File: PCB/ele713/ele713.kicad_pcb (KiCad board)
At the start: 2 copper layers, 37 parts, among them T1 Vi = 36-72V, Vo = 12V / 1.25A, U1 LM5012, U2 LT8304

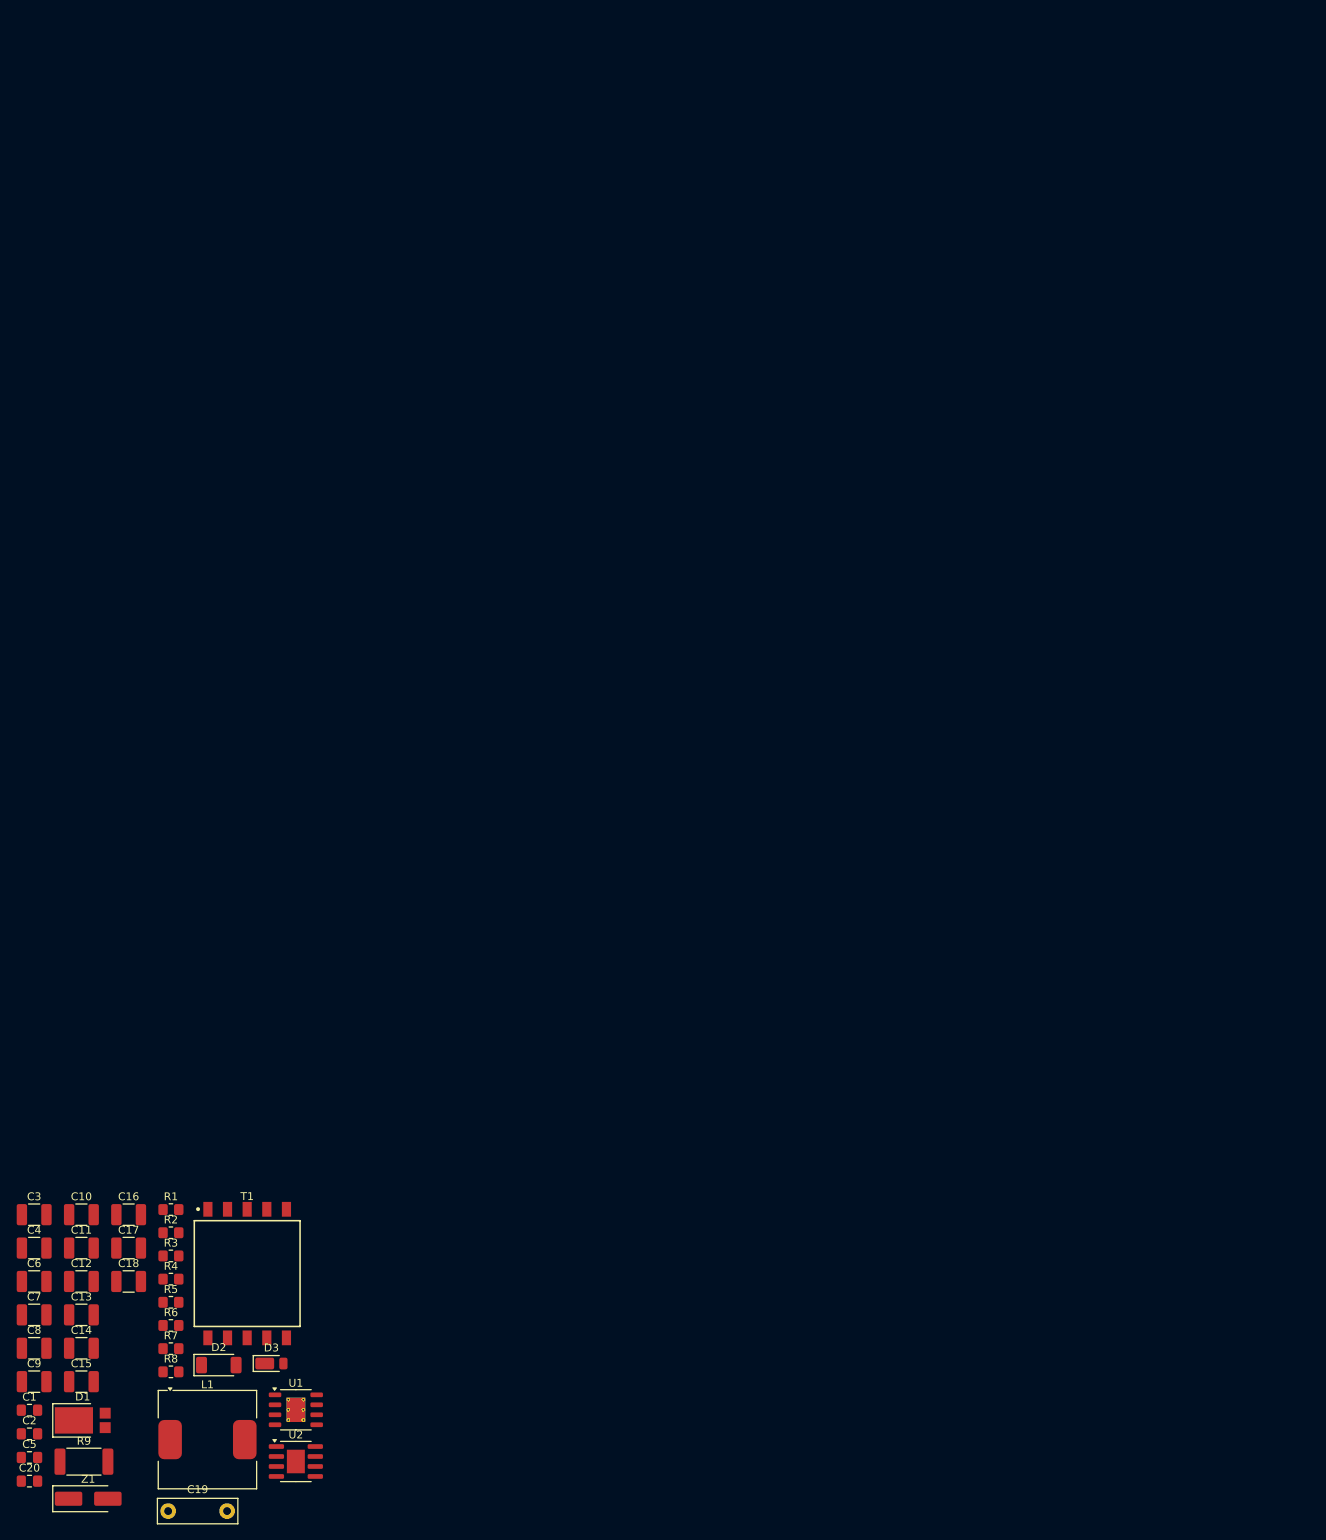
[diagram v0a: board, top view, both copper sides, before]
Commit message: libraries added, schematic fully completed except terminals
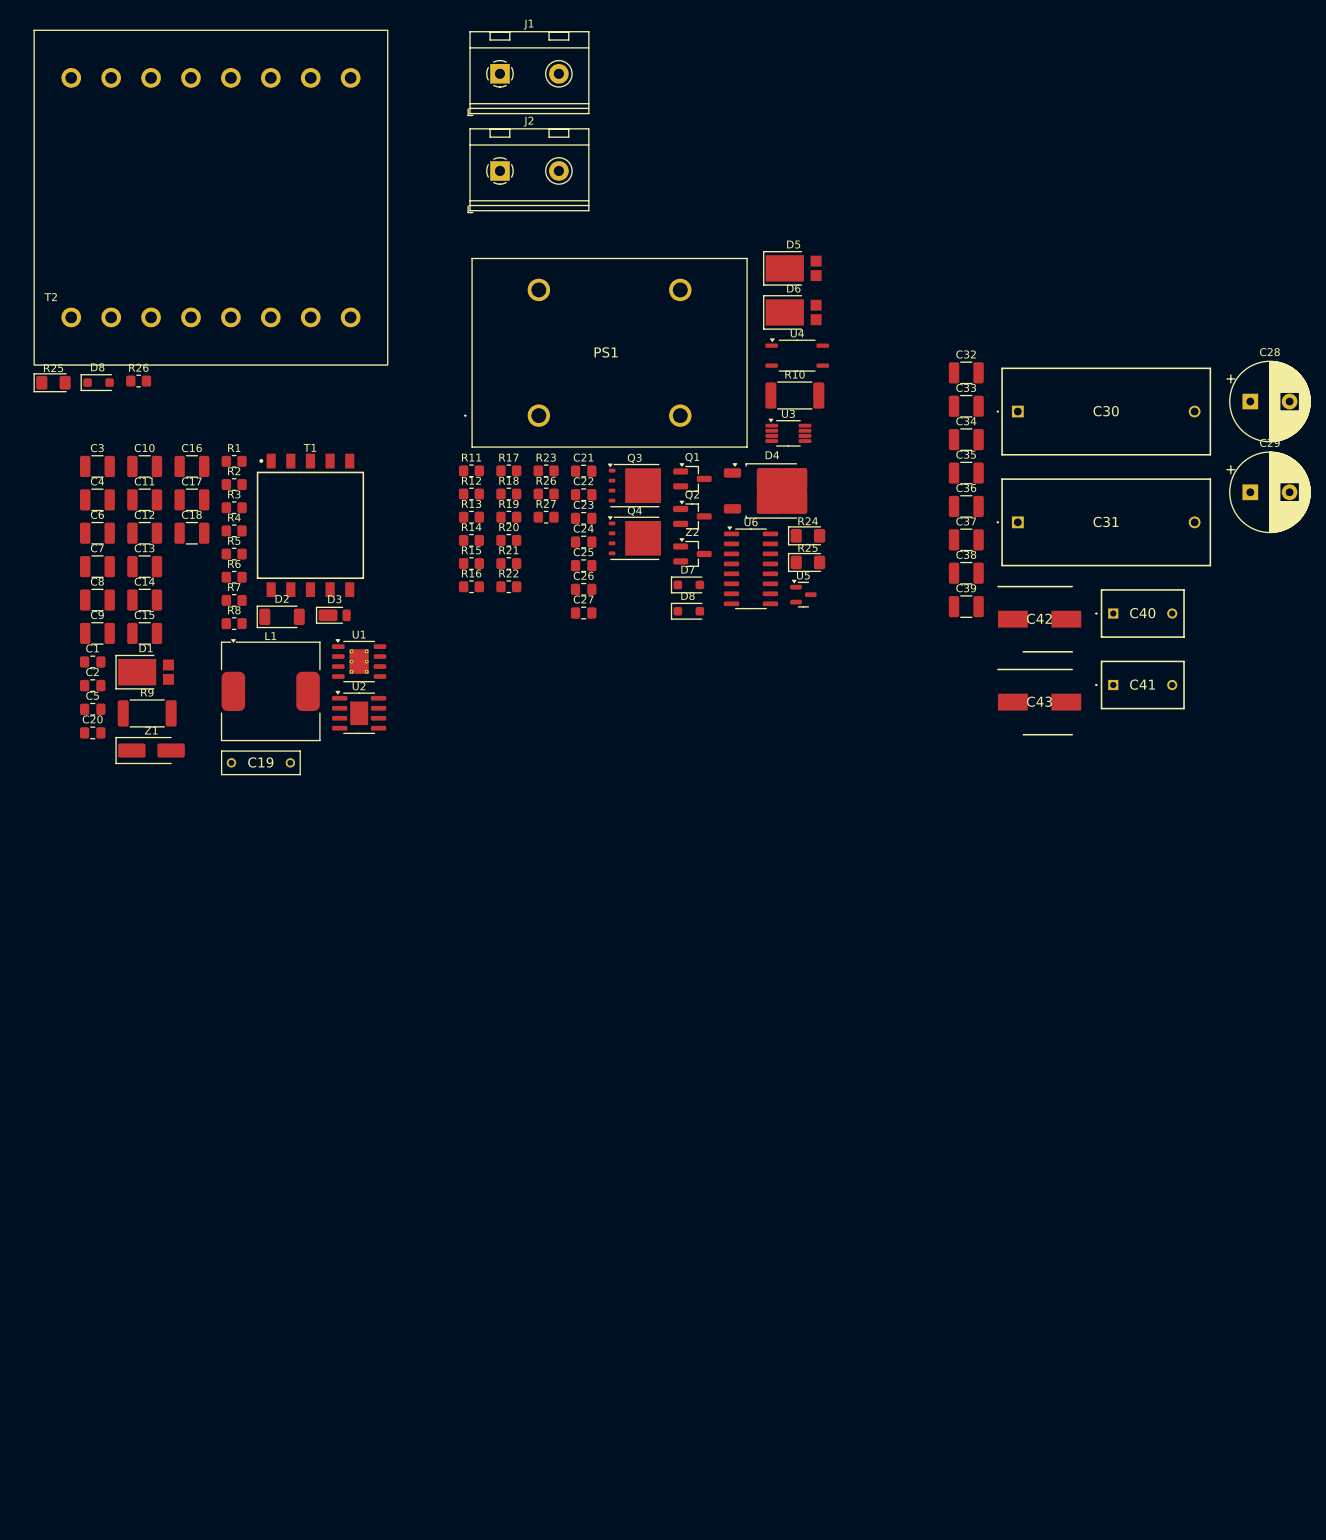
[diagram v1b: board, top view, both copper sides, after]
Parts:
- added C21: 4.7u, Capacitor_SMD:C_0805_2012Metric_Pad1.18x1.45mm_HandSolder, F.Cu at (122.2, -47.9)
- added C22: 6.8n, Capacitor_SMD:C_0805_2012Metric_Pad1.18x1.45mm_HandSolder, F.Cu at (122.2, -44.9)
- added C23: 10n, Capacitor_SMD:C_0805_2012Metric_Pad1.18x1.45mm_HandSolder, F.Cu at (122.2, -41.9)
- added C24: 10n, Capacitor_SMD:C_0805_2012Metric_Pad1.18x1.45mm_HandSolder, F.Cu at (122.2, -38.9)
- added C25: 470p, Capacitor_SMD:C_0805_2012Metric_Pad1.18x1.45mm_HandSolder, F.Cu at (122.2, -35.9)
- added C26: 100p, Capacitor_SMD:C_0805_2012Metric_Pad1.18x1.45mm_HandSolder, F.Cu at (122.2, -32.9)
- added C27: 1u, Capacitor_SMD:C_0805_2012Metric_Pad1.18x1.45mm_HandSolder, F.Cu at (122.2, -29.9)
- added C28: 22u, Capacitor_THT:CP_Radial_D10.0mm_P5.00mm, F.Cu at (207.0, -56.8)
- added C29: 22u, Capacitor_THT:CP_Radial_D10.0mm_P5.00mm, F.Cu at (207.0, -45.2)
- added C30: 3.3u, powerlabLibrary:R46KN410050N1K, F.Cu at (177.4, -55.5)
- added C31: 3.3u, powerlabLibrary:R46KN410050N1K, F.Cu at (177.4, -41.4)
- added C32: 4.7u, Capacitor_SMD:C_1210_3225Metric_Pad1.33x2.70mm_HandSolder, F.Cu at (170.8, -60.4)
- added C33: 4.7u, Capacitor_SMD:C_1210_3225Metric_Pad1.33x2.70mm_HandSolder, F.Cu at (170.8, -56.2)
- added C34: 4.7u, Capacitor_SMD:C_1210_3225Metric_Pad1.33x2.70mm_HandSolder, F.Cu at (170.8, -51.9)
- added C35: 4.7u, Capacitor_SMD:C_1210_3225Metric_Pad1.33x2.70mm_HandSolder, F.Cu at (170.8, -47.7)
- added C36: 22u, Capacitor_SMD:C_1210_3225Metric_Pad1.33x2.70mm_HandSolder, F.Cu at (170.8, -43.4)
- added C37: 22u, Capacitor_SMD:C_1210_3225Metric_Pad1.33x2.70mm_HandSolder, F.Cu at (170.8, -39.2)
- added C38: 22u, Capacitor_SMD:C_1210_3225Metric_Pad1.33x2.70mm_HandSolder, F.Cu at (170.8, -34.9)
- added C39: 22u, Capacitor_SMD:C_1210_3225Metric_Pad1.33x2.70mm_HandSolder, F.Cu at (170.8, -30.7)
- added C40: 2.2u, powerlabLibrary:F861KM473M310A, F.Cu at (189.6, -29.8)
- added C41: 2.2u, powerlabLibrary:F861KM473M310A, F.Cu at (189.6, -20.7)
- added C42: 220u, powerlabLibrary:CAPAE830X1250N, F.Cu at (180.2, -29.1)
- added C43: 220u, powerlabLibrary:CAPAE830X1250N, F.Cu at (180.2, -18.5)
- added D4: V35PWL63, Package_TO_SOT_SMD:TO-252-2, F.Cu at (146.1, -45.4)
- added D5: SDT5H100LP5, powerlabLibrary:D_PowerDI-5, F.Cu at (148.9, -73.7)
- added D6: SDT5H100LP5, powerlabLibrary:D_PowerDI-5, F.Cu at (148.9, -68.1)
- added D7: BZT52H-A18-QX, Diode_SMD:D_SOD-123F, F.Cu at (135.5, -33.5)
- added D8: BZT52H-A18-QX, Diode_SMD:D_SOD-123F, F.Cu at (60.4, -59.2)
- added D8: BZT52H-A18-QX, Diode_SMD:D_SOD-123F, F.Cu at (135.5, -30.1)
- added J1: Conn_01x02_Pin, TerminalBlock_RND:TerminalBlock_RND_205-00067_1x02_P7.50mm_Horizontal, F.Cu at (111.5, -98.5)
- added J2: Conn_01x02_Pin, TerminalBlock_RND:TerminalBlock_RND_205-00067_1x02_P7.50mm_Horizontal, F.Cu at (111.5, -86.1)
- added PS1: SC-18-10J, powerlabLibrary:SC1810J, F.Cu at (116.5, -55.0)
- added Q1: PMBT2222A-Q, Package_TO_SOT_SMD:SOT-23_Handsoldering, F.Cu at (136.0, -47.0)
- added Q2: PMBT2907A-Q, Package_TO_SOT_SMD:SOT-23_Handsoldering, F.Cu at (136.0, -42.2)
- added Q3: BSC096N10LS5, Package_TO_SOT_SMD:TDSON-8-1, F.Cu at (128.7, -46.1)
- added Q4: BSC096N10LS5, Package_TO_SOT_SMD:TDSON-8-1, F.Cu at (128.7, -39.4)
- added R10: 4m, Resistor_SMD:R_2512_6332Metric_Pad1.40x3.35mm_HandSolder, F.Cu at (149.0, -57.6)
- added R11: 10k, Resistor_SMD:R_0805_2012Metric_Pad1.20x1.40mm_HandSolder, F.Cu at (107.9, -48.0)
- added R12: 1.1M, Resistor_SMD:R_0805_2012Metric_Pad1.20x1.40mm_HandSolder, F.Cu at (107.9, -45.0)
- added R13: 12k, Resistor_SMD:R_0805_2012Metric_Pad1.20x1.40mm_HandSolder, F.Cu at (107.9, -42.1)
- added R14: 3.83k, Resistor_SMD:R_0805_2012Metric_Pad1.20x1.40mm_HandSolder, F.Cu at (107.9, -39.1)
- added R15: 16.5k, Resistor_SMD:R_0805_2012Metric_Pad1.20x1.40mm_HandSolder, F.Cu at (107.9, -36.2)
- added R16: 4.99k, Resistor_SMD:R_0805_2012Metric_Pad1.20x1.40mm_HandSolder, F.Cu at (107.9, -33.2)
- added R17: 1k, Resistor_SMD:R_0805_2012Metric_Pad1.20x1.40mm_HandSolder, F.Cu at (112.6, -48.0)
- added R18: 1k, Resistor_SMD:R_0805_2012Metric_Pad1.20x1.40mm_HandSolder, F.Cu at (112.6, -45.0)
- added R19: 680R, Resistor_SMD:R_0805_2012Metric_Pad1.20x1.40mm_HandSolder, F.Cu at (112.6, -42.1)
- added R20: 10k, Resistor_SMD:R_0805_2012Metric_Pad1.20x1.40mm_HandSolder, F.Cu at (112.6, -39.1)
- added R21: 39k, Resistor_SMD:R_0805_2012Metric_Pad1.20x1.40mm_HandSolder, F.Cu at (112.6, -36.2)
- added R22: 9.53k, Resistor_SMD:R_0805_2012Metric_Pad1.20x1.40mm_HandSolder, F.Cu at (112.6, -33.2)
- added R23: 2.49k, Resistor_SMD:R_0805_2012Metric_Pad1.20x1.40mm_HandSolder, F.Cu at (117.4, -48.0)
- added R24: 10R, Diode_SMD:D_1206_3216Metric_Pad1.42x1.75mm_HandSolder, F.Cu at (150.7, -39.7)
- added R25: 10R, Diode_SMD:D_1206_3216Metric_Pad1.42x1.75mm_HandSolder, F.Cu at (150.7, -36.3)
- added R25: 10R, Diode_SMD:D_1206_3216Metric_Pad1.42x1.75mm_HandSolder, F.Cu at (54.7, -59.2)
- added R26: 100k, Resistor_SMD:R_0805_2012Metric_Pad1.20x1.40mm_HandSolder, F.Cu at (65.5, -59.4)
- added R26: 100k, Resistor_SMD:R_0805_2012Metric_Pad1.20x1.40mm_HandSolder, F.Cu at (117.4, -45.0)
- added R27: 100k, Resistor_SMD:R_0805_2012Metric_Pad1.20x1.40mm_HandSolder, F.Cu at (117.4, -42.1)
- added T2: ELE713 Transformer, powerlabLibrary:ETD39_coilformer, F.Cu at (56.9, -67.5)
- added U3: UCC28C55, powerlabLibrary:VSSOP-8_3x3mm_P0.65mm, F.Cu at (148.2, -52.7)
- added U4: ISOM8110, powerlabLibrary:SOIC-4_4.55x3.7mm_P2.54mm, F.Cu at (149.3, -62.6)
- added U5: TL431DBZ, Package_TO_SOT_SMD:SOT-23, F.Cu at (150.1, -32.2)
- added U6: 2EDB8259F, Package_SO:SOIC-16_3.9x9.9mm_P1.27mm, F.Cu at (143.4, -35.5)
- added Z2: BZX84-A10,215, Package_TO_SOT_SMD:SOT-23_Handsoldering, F.Cu at (136.0, -37.4)
- C19: footprint Capacitor_THT:C_Rect_L10.0mm_W3.0mm_P7.50mm_MKS4 -> powerlabLibrary:R76QD0220SE00J
- D1: footprint Diode_SMD:D_PowerDI-5 -> powerlabLibrary:D_PowerDI-5
- moved C1 95.6 mm to (59.7, -23.7)
- moved C10 95.6 mm to (66.3, -48.5)
- moved C11 95.6 mm to (66.3, -44.3)
- moved C12 95.6 mm to (66.3, -40.0)
- moved C13 95.6 mm to (66.3, -35.8)
- moved C14 95.6 mm to (66.3, -31.5)
- moved C15 95.6 mm to (66.3, -27.3)
- moved C16 95.6 mm to (72.3, -48.5)
- moved C17 95.6 mm to (72.3, -44.3)
- moved C18 95.6 mm to (72.3, -40.0)
- moved C19 95.6 mm to (77.3, -10.8)
- moved C2 95.6 mm to (59.7, -20.6)
- moved C20 95.6 mm to (59.7, -14.6)
- moved C3 95.6 mm to (60.3, -48.5)
- moved C4 95.6 mm to (60.3, -44.3)
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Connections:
- T1 pad 1: (no net) -> unconnected-(T1-Pad1)
- T1 pad 2: (no net) -> unconnected-(T1-Pad2)
- T1 pad 4: (no net) -> unconnected-(T1-Pad4)
- T1 pad 8: (no net) -> unconnected-(T1-Pad8)

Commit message: pcb v1 is uploaded
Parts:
- removed the D8 at (135.5, -30.1)
- removed the R25 at (150.7, -36.3)
- removed the R26 at (117.4, -45.0)
- C11, C14, C16, C18, C32, C33, C36, C38, D5, D6, Q3, Q4: moved to B.Cu
- T1: footprint powerlabLibrary:WE-FLYLT_EP13_L13.46W17.75H12.70 -> KiCad Library:WE-FLYLT_EP13_L13.46W17.75H12.70
- moved J2 242.0 mm to (277.0, 90.5), turned to 90 degrees
- moved J1 206.5 mm to (22.6, 88.0), turned to -90 degrees
- moved C28 197.8 mm to (74.4, 89.9), turned to -90 degrees
- moved R23 197.5 mm to (216.3, 123.0)
- moved T2 197.5 mm to (193.9, 74.7), turned to -90 degrees
- moved R17 193.4 mm to (210.7, 118.8), turned to 180 degrees
- moved R25 191.6 mm to (166.7, 96.2)
- moved D8 191.4 mm to (170.4, 97.4), turned to -90 degrees
- moved U4 189.9 mm to (196.4, 121.3)
- moved R26 189.6 mm to (172.7, 97.0), turned to -90 degrees
- moved C23 186.3 mm to (212.1, 121.2)
- moved R19 186.1 mm to (206.3, 118.8)
- moved C29 184.8 mm to (74.4, 83.5), turned to 90 degrees
- moved R22 184.3 mm to (215.3, 119.8), turned to -90 degrees
- moved R21 183.9 mm to (207.9, 121.2)
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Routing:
- net VIN: track 0.00 -> 0.89 mm
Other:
- board outline added: 225.7 x 84.2 mm
